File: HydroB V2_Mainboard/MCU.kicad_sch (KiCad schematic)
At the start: 13 parts, among them U1 ESP32-S3-WROOM-1-N16R2

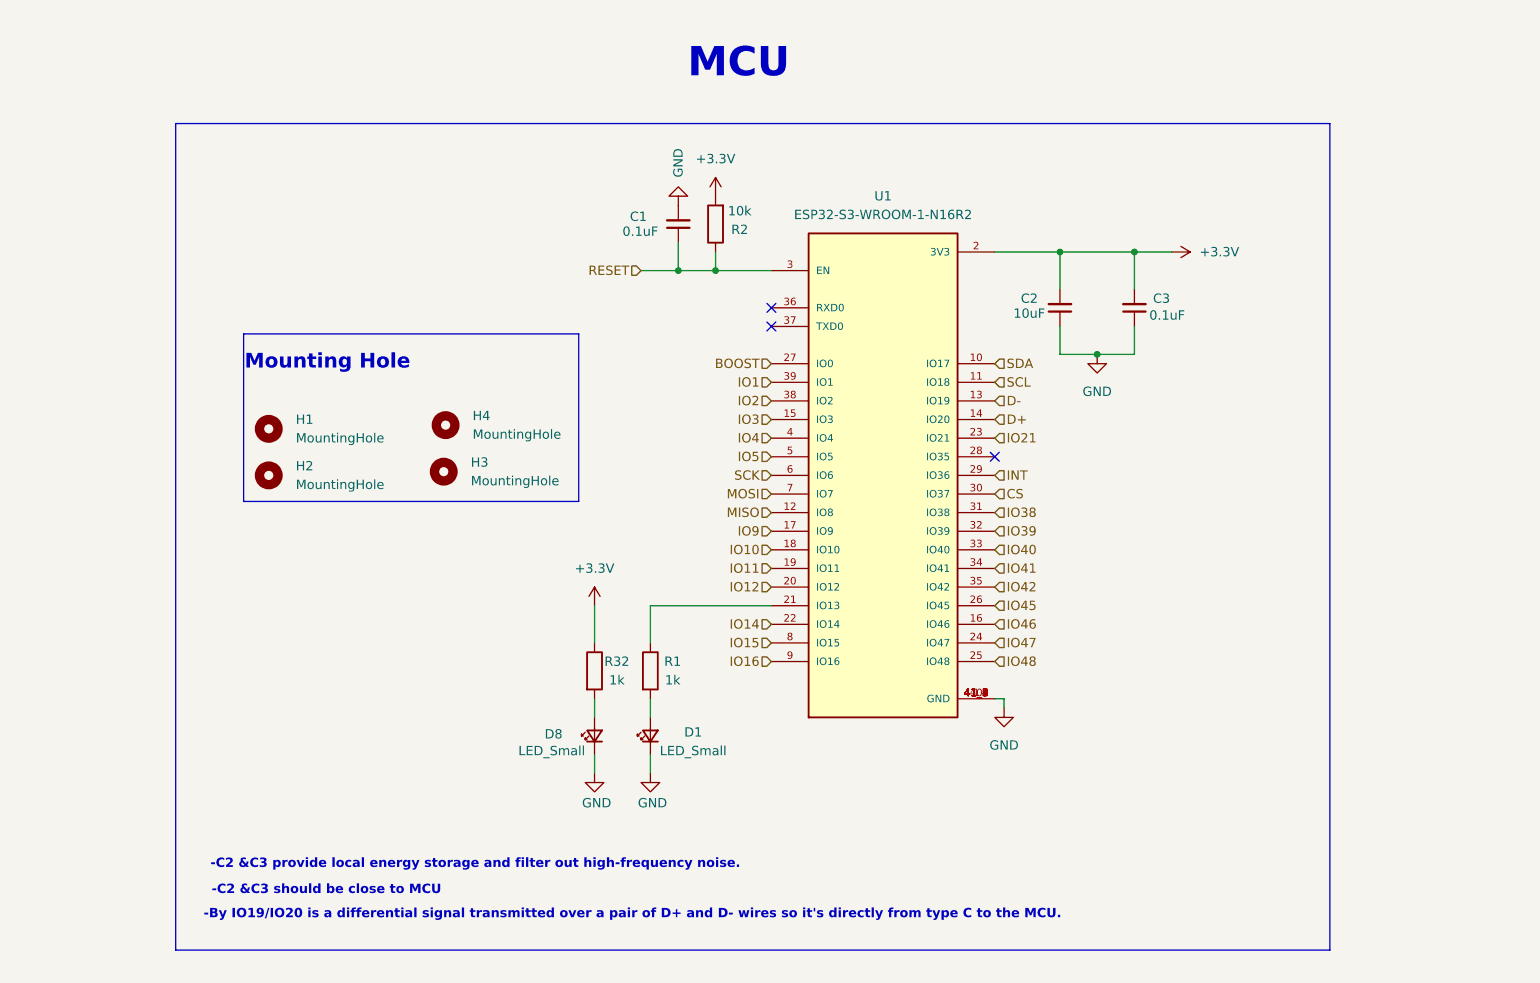
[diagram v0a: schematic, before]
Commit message: Update LCD schematic
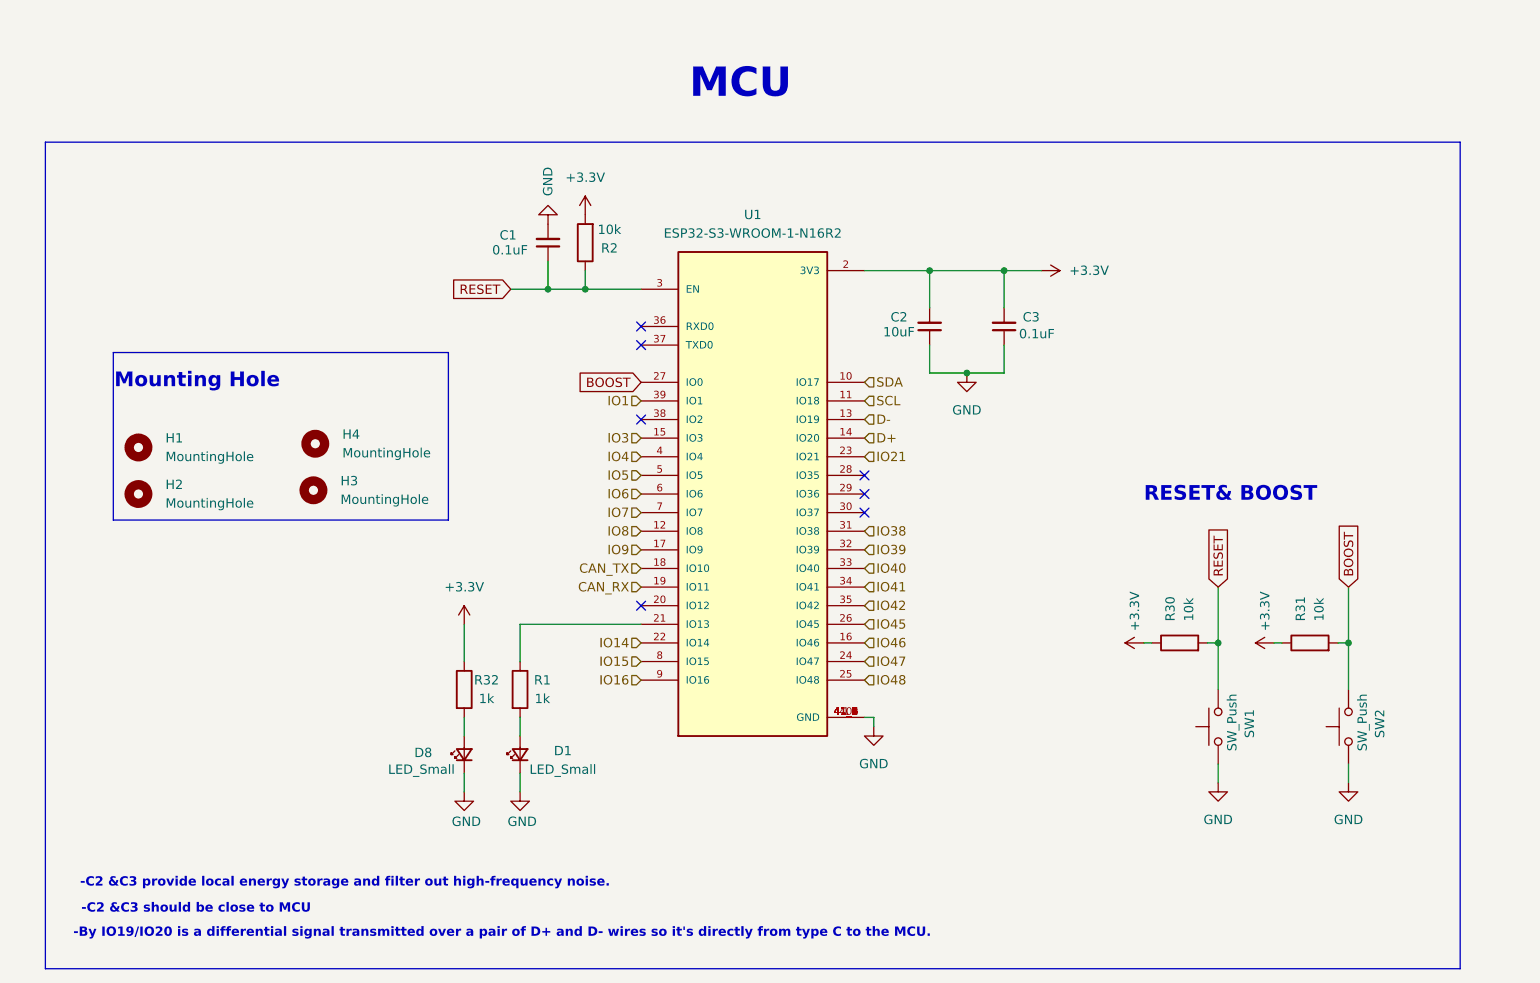
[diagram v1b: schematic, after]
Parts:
- added R30, R31: 10k, Resistor_SMD:R_0603_1608Metric, symbol Device:R
- added SW1, SW2: SW_Push, Button_Switch_SMD:SW_Push_1P1T_NO_CK_KMR2, symbol Switch:SW_Push
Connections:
- net +3.3V: now also R30.1, R31.1
- net GND: now also SW1.1, SW2.1
- net RESET: now also R30.2, SW1.2
- net BOOST renamed BOOST 
- net BOOST : now also R31.2, SW2.2
- net CS: no longer names the net of U1.30 (IO37)
- net INT: no longer names the net of U1.29 (IO36)
- net IO10 renamed CAN_TX
- net IO11 renamed CAN_RX
- net IO12: no longer names the net of U1.20 (IO12)
- net IO2: no longer names the net of U1.38 (IO2)
- net MISO renamed IO8
- net MOSI renamed IO7
- net SCK renamed IO6
- no-connect marks 3 -> 7
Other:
- note added: "RESET& BOOST"
- moved on the sheet: C1, C2, C3, D1, D8, H1, H2, H3, H4, R1, R2, R32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

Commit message: mainboard updated
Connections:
- net IO35: now reaches U1.28 (IO35)
- no-connect marks 7 -> 6
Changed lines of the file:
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@@
-	)
-	(no_connect
-		(at 157.48 91.44)
 	)
 	(no_connect
@@
 		)
 	)
+	(hierarchical_label "IO35"
+		(shape input)
+		(at 157.48 91.44 0)
+		(fields_autoplaced yes)
+		(effects
+			(font
+				(size 1.27 1.27)
+			)
+			(justify left)
+		)
+	)

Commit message: Schematic mainboard update
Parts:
- removed D1: LED_Small, LED_SMD:LED_0805_2012Metric, symbol Device:LED_Small
- removed R1: 1k, Resistor_SMD:R_0603_1608Metric, symbol Device:R
- SW1, SW2: footprint Button_Switch_SMD:SW_Push_1P1T_NO_CK_KMR2 -> Button_Switch_SMD:SW_Push_SPST_NO_Alps_SKRK
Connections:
- net IO41 is gone; now on net SCL: U1.34 (IO41)
- net IO42 is gone; now on net SDA: U1.35 (IO42)
- net SCL: no longer U1.11 (IO18)
- net SDA: no longer U1.10 (IO17)
- net G6: now reaches U1.20 (IO12)
- net G7: now reaches U1.21 (IO13)
- net EN_RS485: now reaches U1.29 (IO36)
- net RS485_RX: now reaches U1.36 (RXD0)
- net RS485_TX: now reaches U1.37 (TXD0)
- net VSYNC: now reaches U1.38 (IO2)
- net CAN_RX renamed G5
- net CAN_TX renamed G4
- net IO1 renamed BL_PWM
- net IO14 renamed B3
- net IO15 renamed R4
- net IO16 renamed R5
- net IO21 renamed B4
- net IO3 renamed R7
- net IO35 renamed BUSY
- net IO38: no longer names the net of U1.31 (IO38)
- net IO39 renamed INT
- net IO4 renamed HSYNC
- net IO40 renamed RST
- net IO45 renamed B7
- net IO46 renamed G2
- net IO47 renamed B5
- net IO48 renamed B6
- net IO5 renamed LCD DE
- net IO6 renamed LCD_PCLK
- net IO7 renamed R3
- net IO8 renamed R6
- net IO9 renamed G3
- new net RX: U1.11 (IO18)
- new net TX: U1.10 (IO17)
- no-connect marks 6 -> 2
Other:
- moved on the sheet: C1, C2, C3, D8, H1, H2, H3, H4, R2, R30, R31, R32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

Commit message: Mainboard schematic update
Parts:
- removed H1, H2, H3, H4: MountingHole, MountingHole:MountingHole_3mm_Pad_Via, symbol Mechanical:MountingHole
- added D1: LED_Small, LED_SMD:LED_0805_2012Metric, symbol Device:LED_Small
- added R1: 1k, Resistor_SMD:R_0603_1608Metric, symbol Device:R
- added TP3, TP4: TestPoint, TestPoint:TestPoint_Loop_D1.80mm_Drill1.0mm_Beaded, symbol Connector:TestPoint
- C3: value 0.1uF -> 100nF
- SW1: footprint Button_Switch_SMD:SW_Push_SPST_NO_Alps_SKRK -> Button_Switch_THT:SW_Tactile_SPST_Angled_PTS645Vx39-2LFS
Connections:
- net R5 is gone; now on net EN_RS485: U1.9 (IO16)
- net RX is gone; now on net RS485_RX: U1.11 (IO18)
- net TX is gone; now on net RS485_TX: U1.10 (IO17)
- net EN_RS485: no longer U1.29 (IO36)
- net GND: now also D1.1 (K)
- net RS485_RX: now also TP4.1; no longer U1.36 (RXD0)
- net RS485_TX: now also TP3.1; no longer U1.37 (TXD0)
- net B3: no longer names the net of U1.22 (IO14)
- net B4: no longer names the net of U1.23 (IO21)
- net B5: no longer names the net of U1.24 (IO47)
- net B6 renamed LED1
- net B7: no longer names the net of U1.26 (IO45)
- net BL_PWM: no longer names the net of U1.39 (IO1)
- net BUSY: no longer names the net of U1.28 (IO35)
- net G2: no longer names the net of U1.16 (IO46)
- net G3: no longer names the net of U1.17 (IO9)
- net G4 renamed LED2
- net G5: no longer names the net of U1.19 (IO11)
- net G6: no longer names the net of U1.20 (IO12)
- net G7: no longer names the net of U1.21 (IO13)
- net HSYNC: no longer names the net of U1.4 (IO4)
- net INT: no longer names the net of U1.32 (IO39)
- net LCD DE: no longer names the net of U1.5 (IO5)
- net LCD_PCLK: no longer names the net of U1.6 (IO6)
- net R3 renamed RXD
- net R4: no longer names the net of U1.8 (IO15)
- net R6 renamed TXD
- net R7: no longer names the net of U1.15 (IO3)
- net RST: no longer names the net of U1.33 (IO40)
- net SCL: no longer names the net of U1.34 (IO41)
- net SDA: no longer names the net of U1.35 (IO42)
- net VSYNC renamed LED
- net LED: now also R1.1
- new net: D1.2 (A), R1.2
- no-connect marks 2 -> 25
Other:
- note removed: "Mounting Hole"
- moved on the sheet: C1, C2, C3, D8, R2, R30, R31, R32, SW1, SW2, U1

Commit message: main PCB board placement
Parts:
- removed R2: 10k, Resistor_SMD:R_0603_1608Metric, symbol Device:R
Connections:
- net UART_TX: now reaches U1.36 (RXD0)
- net UART_RX: now reaches U1.37 (TXD0)
- net BOOST  renamed BOOT
- net D+: no longer names the net of U1.14 (IO20)
- net D-: no longer names the net of U1.13 (IO19)
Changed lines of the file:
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@@
-	)
-	(junction
-		(at 71.12 64.77)
-		(diameter 0)
-		(color 0 0 0 0)
 	)
 	(junction
@@
 	)
 	(no_connect
+		(at 109.22 82.55)
+	)
+	(no_connect
 		(at 78.74 80.01)
 	)
@@
 	)
 	(no_connect
-		(at 78.74 72.39)
-	)
-	(no_connect
 		(at 109.22 97.79)
-	)
-	(no_connect
-		(at 78.74 69.85)
 	)
 	(no_connect
@@
 	)
 	(no_connect
+		(at 109.22 85.09)
+	)
+	(no_connect
 		(at 109.22 102.87)
 	)
@@
 	(wire
 		(pts
-			(xy 71.12 64.77) (xy 78.74 64.77)
-		)
-		(stroke
-			(width 0)
-			(type default)
-		)
-	)
-	(wire
-		(pts
-			(xy 71.12 62.23) (xy 71.12 64.77)
-		)
-		(stroke
-			(width 0)
-			(type default)
-		)
-	)
-	(wire
-		(pts
 			(xy 110.49 123.19) (xy 109.22 123.19)
 		)
@@
 	(wire
 		(pts
-			(xy 66.04 64.77) (xy 71.12 64.77)
+			(xy 66.04 64.77) (xy 78.74 64.77)
 		)
 		(stroke
@@
 				(thickness 0.254)
 				(bold yes)
-			)
-		)
-	)
-	(global_label "BOOST "
-		(shape input)
-		(at 234.95 66.04 90)
-		(fields_autoplaced yes)
-		(effects
-			(font
-				(size 1.27 1.27)
-			)
-			(justify left)
-		)
-		(property "Intersheetrefs" "${INTERSHEET_REFS}"
-			(at 234.95 55.9791 90)
-			(effects
-				(font
-					(size 1.27 1.27)
-				)
-				(justify left)
-				(hide yes)
-			)
-		)
-	)
-	(global_label "BOOST "
-		(shape input)
-		(at 78.74 77.47 180)
-		(fields_autoplaced yes)
-		(effects
-			(font
-				(size 1.27 1.27)
-			)
-			(justify right)
-		)
-		(property "Intersheetrefs" "${INTERSHEET_REFS}"
-			(at 68.6791 77.47 0)
-			(effects
-				(font
-					(size 1.27 1.27)
-				)
-				(justify right)
-				(hide yes)
 			)
 		)
@@
 		)
 	)
-	(global_label "RESET"
-		(shape input)
-		(at 214.63 66.04 90)
-		(fields_autoplaced yes)
-		(effects
-			(font
-				(size 1.27 1.27)
-			)
-			(justify left)
-		)
-		(property "Intersheetrefs" "${INTERSHEET_REFS}"
-			(at 214.63 57.3097 90)
-			(effects
-				(font
-					(size 1.27 1.27)
-				)
-				(justify left)
-				(hide yes)
-			)
-		)
-	)
-	(global_label "RESET"
-		(shape input)
-		(at 60.96 64.77 180)
-		(fields_autoplaced yes)
-		(effects
-			(font
-				(size 1.27 1.27)
-			)
-			(justify right)
-		)
-		(property "Intersheetrefs" "${INTERSHEET_REFS}"
-			(at 52.2297 64.77 0)
-			(effects
-				(font
-					(size 1.27 1.27)
-				)
-				(justify right)
-				(hide yes)
-			)
-		)
-	)
 	(global_label "LED"
 		(shape input)
@@
 		)
 	)
-	(hierarchical_label "D+"
+	(hierarchical_label "BOOT"
 		(shape input)
-		(at 109.22 85.09 0)
+		(at 78.74 77.47 180)
 		(fields_autoplaced yes)
 		(effects
@@
 				(size 1.27 1.27)
 			)
-			(justify left)
+			(justify right)
 		)
 	)
@@
 		)
 	)
+	(hierarchical_label "UART_TX"
+		(shape input)
+		(at 78.74 69.85 180)
+		(fields_autoplaced yes)
+		(effects
+			(font
+				(size 1.27 1.27)
+			)
+			(justify right)
+		)
+	)
+	(hierarchical_label "BOOT"
+		(shape input)
+		(at 234.95 66.04 90)
+		(fields_autoplaced yes)
+		(effects
+			(font
+				(size 1.27 1.27)
+			)
+			(justify left)
+		)
+	)
 	(hierarchical_label "RS485_RX"
 		(shape input)
@@
 		)
 	)
-	(hierarchical_label "D-"
-		(shape input)
-		(at 109.22 82.55 0)
-		(fields_autoplaced yes)
-		(effects
-			(font
-				(size 1.27 1.27)
-			)
-			(justify left)
-		)
-	)
 	(hierarchical_label "TXD"
 		(shape input)
@@
 		)
 	)
+	(hierarchical_label "UART_RX"
+		(shape input)
+		(at 78.74 72.39 180)
+		(fields_autoplaced yes)
+		(effects
+			(font
+				(size 1.27 1.27)
+			)
+			(justify right)
+		)
+	)
 	(hierarchical_label "RXD"
 		(shape input)
@@
 		)
 	)
+	(hierarchical_label "RESET"
+		(shape input)
+		(at 60.96 64.77 180)
+		(fields_autoplaced yes)
+		(effects
+			(font
+				(size 1.27 1.27)
+			)
+			(justify right)
+		)
+	)
 	(hierarchical_label "LED2"
 		(shape input)
@@
 		)
 	)
+	(hierarchical_label "RESET"
+		(shape input)
+		(at 214.63 66.04 90)
+		(fields_autoplaced yes)
+		(effects
+			(font
+				(size 1.27 1.27)
+			)
+			(justify left)
+		)
+	)
 	(hierarchical_label "EN_RS485"
 		(shape input)
@@
 	)
 	(symbol
-		(lib_id "power:+3.3V")
-		(at 71.12 54.61 0)
-		(unit 1)
-		(exclude_from_sim no)
-		(in_bom yes)
-		(on_board yes)
-		(dnp no)
-		(fields_autoplaced yes)
-		(property "Reference" "#PWR03"
-			(at 71.12 58.42 0)
-			(effects
-				(font
-					(size 1.27 1.27)
-				)
-				(hide yes)
-			)
-		)
-		(property "Value" "+3.3V"
-			(at 71.12 49.53 0)
-			(effects
-				(font
-					(size 1.27 1.27)
-				)
-			)
-		)
-		(property "Footprint" ""
-			(at 71.12 54.61 0)
-			(effects
-				(font
-					(size 1.27 1.27)
-				)
-				(hide yes)
-			)
-		)
-		(property "Datasheet" ""
-			(at 71.12 54.61 0)
-			(effects
-				(font
-					(size 1.27 1.27)
-				)
-				(hide yes)
-			)
-		)
-		(property "Description" "Power symbol creates a global label with name \"+3.3V\""
-			(at 71.12 54.61 0)
-			(effects
-				(font
-					(size 1.27 1.27)
-				)
-				(hide yes)
-			)
-		)
-		(pin "1"
-		)
-		(instances
-			(project "LCD High Revolution"
-				(path "/7eaed49e-949c-4b32-bb59-42041e199453/cb3a589e-3872-4cde-9770-3d39d4934022/0070a5fd-2242-49a9-8515-77361d4f22c9"
-					(reference "#PWR03")
-					(unit 1)
-				)
-			)
-		)
-	)
-	(symbol
 		(lib_id "power:GND")
 		(at 110.49 124.46 0)
@@
 					(unit 1)
 				)
-			)
-		)
-	)
-	(symbol
-		(lib_id "Device:R")
-		(at 71.12 58.42 180)
-		(unit 1)
-		(exclude_from_sim no)
-		(in_bom yes)
-		(on_board yes)
-		(dnp no)
-		(property "Reference" "R2"
-			(at 74.422 59.182 0)
-			(effects
-				(font
-					(size 1.27 1.27)
-				)
-			)
-		)
-		(property "Value" "10k"
-			(at 74.422 56.642 0)
-			(effects
-				(font
-					(size 1.27 1.27)
-				)
-			)
-		)
-		(property "Footprint" "Resistor_SMD:R_0603_1608Metric"
-			(at 72.898 58.42 90)
-			(effects
-				(font
-					(size 1.27 1.27)
-				)
-				(hide yes)
-			)
-		)
-		(property "Datasheet" "~"
-			(at 71.12 58.42 0)
-			(effects
-				(font
-					(size 1.27 1.27)
-				)
-				(hide yes)
-			)
-		)
-		(property "Description" "Resistor"
-			(at 71.12 58.42 0)
-			(effects
-				(font
-					(size 1.27 1.27)
-				)
-				(hide yes)
-			)
-		)
-		(pin "1"
-		)
-		(pin "2"
-		)
-		(instances
-			(project "LCD High Revolution"
-				(path "/7eaed49e-949c-4b32-bb59-42041e199453/cb3a589e-3872-4cde-9770-3d39d4934022/0070a5fd-2242-49a9-8515-77361d4f22c9"
-					(reference "R2")
-					(unit 1)
-				)

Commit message: PCB placement and ERC
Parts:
- removed U1: ESP32-S3-WROOM-1-N16R2, MOD FILE:XCVR_ESP32-S3-WROOM-1-N16R2, symbol ESP32-S3-WROOM-1-N16R2:ESP32-S3-WROOM-1-N16R2
- added R18: 10k, Resistor_SMD:R_0603_1608Metric, symbol Device:R
- added SW3: SW_Push, Button_Switch_THT:SW_Tactile_SPST_Angled_PTS645Vx39-2LFS, symbol Switch:SW_Push
- added U4: ESP32-S3-WROOM-1-N16R2, ESP32-S3-WROOM-1-N16R2:XCVR_ESP32-S3-WROOM-1-N16R2, symbol ESP32-S3-WROOM-1-N16R2:ESP32-S3-WROOM-1-N16R2
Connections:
- net +3.3V: now also R18.1, U4.2 (3V3)
- net BOOT: now also U4.27 (IO0)
- net EN_RS485: now also U4.9 (IO16)
- net GND: now also SW3.2, U4.1 (GND), U4.40 (GND), U4.41_1 (GND), U4.41_2 (GND), U4.41_3 (GND), U4.41_4 (GND), U4.41_5 (GND), U4.41_6 (GND), U4.41_7 (GND), U4.41_8 (GND), U4.41_9 (GND)
- net LED: now also U4.38 (IO2)
- net LED1: now also U4.25 (IO48)
- net LED2: now also U4.18 (IO10)
- net RESET: now also U4.3 (EN)
- net RS485_RX: now also U4.11 (IO18)
- net RS485_TX: now also U4.10 (IO17)
- net RXD: now also U4.7 (IO7)
- net TXD: now also U4.12 (IO8)
- net UART_RX: now also U4.37 (TXD0)
- net UART_TX: now also U4.36 (RXD0)
- new net: R18.2, SW3.1, U4.26 (IO45)
- no-connect marks 25 -> 24
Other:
- company: (none) -> MCU
- title: (none) -> Prak Chilifong
- moved on the sheet: R30, R31
